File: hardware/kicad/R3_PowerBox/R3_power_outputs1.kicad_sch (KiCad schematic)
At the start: 7 parts, among them J10 BATTERY / CHARGER TELEMETRY, J2 DIGITAL POWER OUT, J3 ISOLATED POWER OUT, J4 CONTROL / SERVICE, J5 PRIMARY AUX DNP, J6 ISOLATED AUX DNP

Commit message: Finalize R3 PowerBox pre-placement corrections
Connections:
- net PD_CONTRACT_12V_N: now reaches J10.10
- net PD_ALERT_N: now reaches J10.9
- no-connect marks 7 -> 5

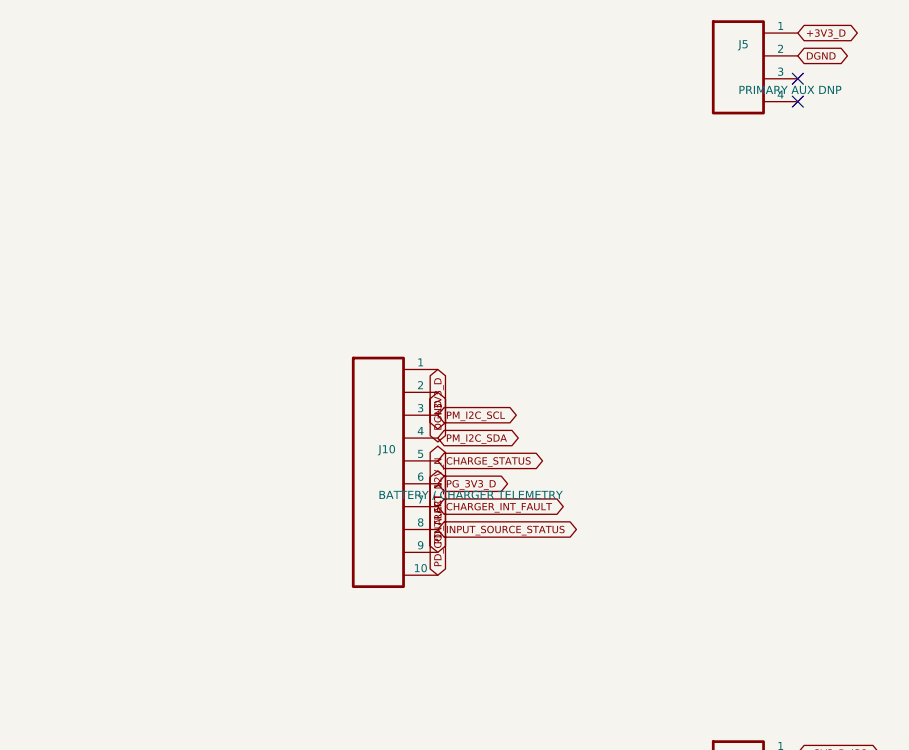
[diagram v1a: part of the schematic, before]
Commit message: Finalize R3 PowerBox pre-routing placement
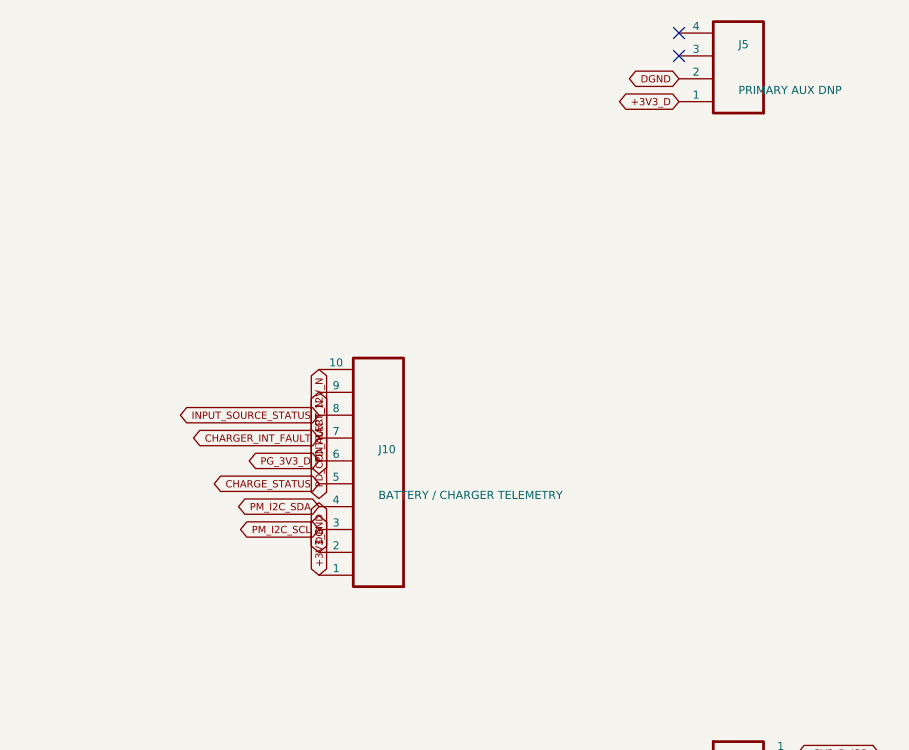
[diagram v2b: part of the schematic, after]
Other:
- moved on the sheet: J10, J5

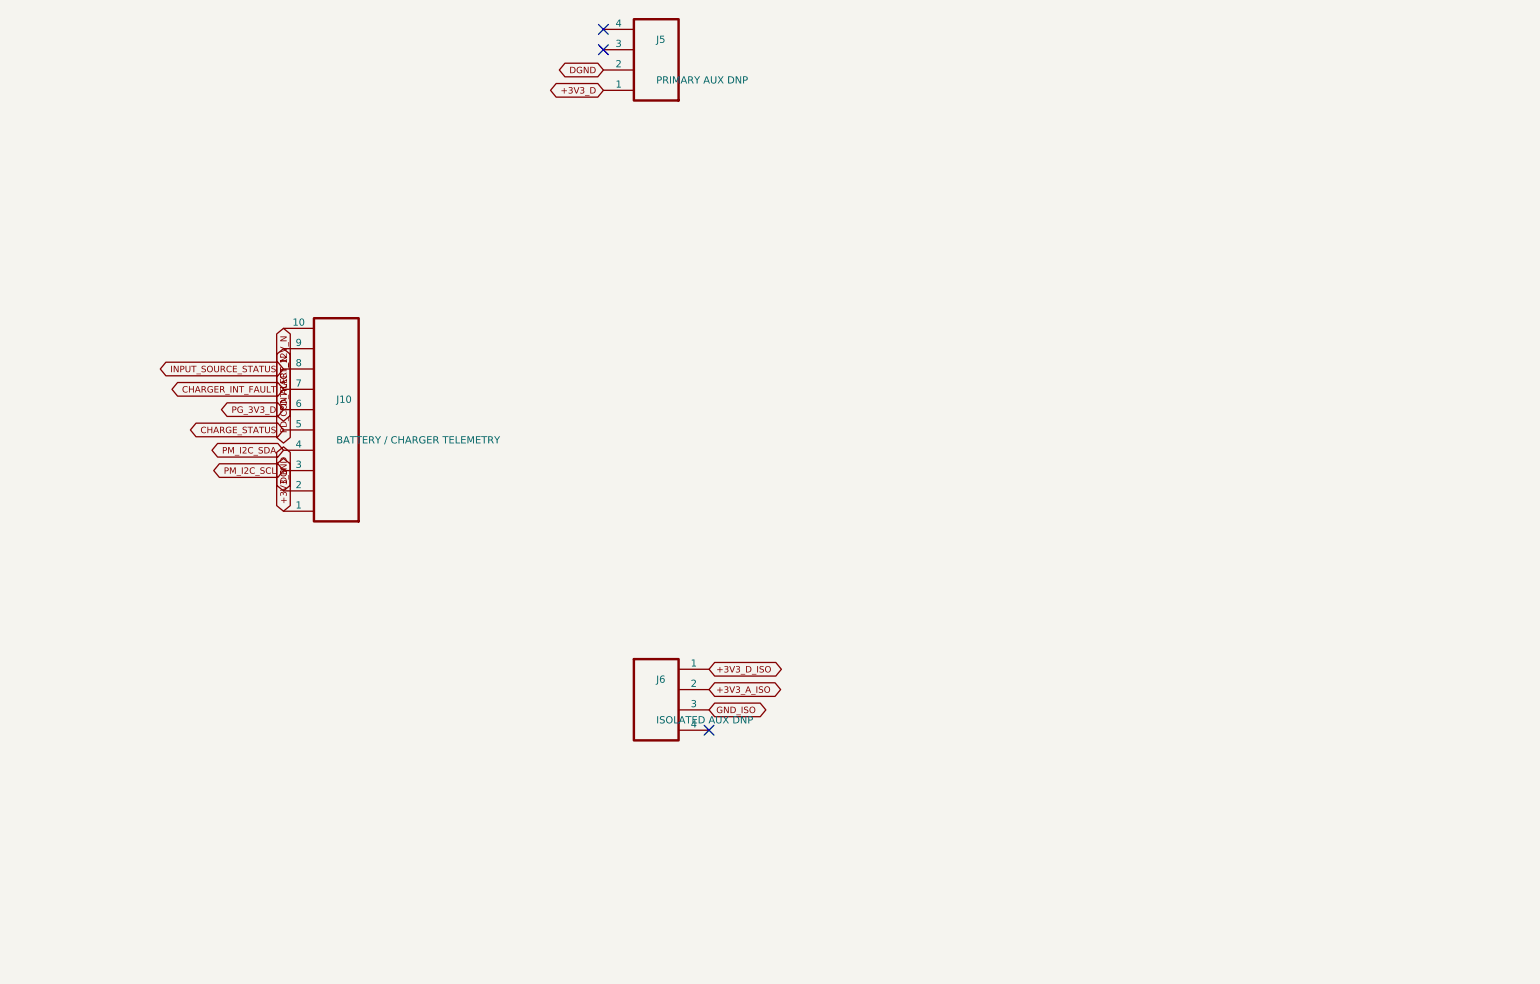
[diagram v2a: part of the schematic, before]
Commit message: Finalize R3 PowerBox user power controls
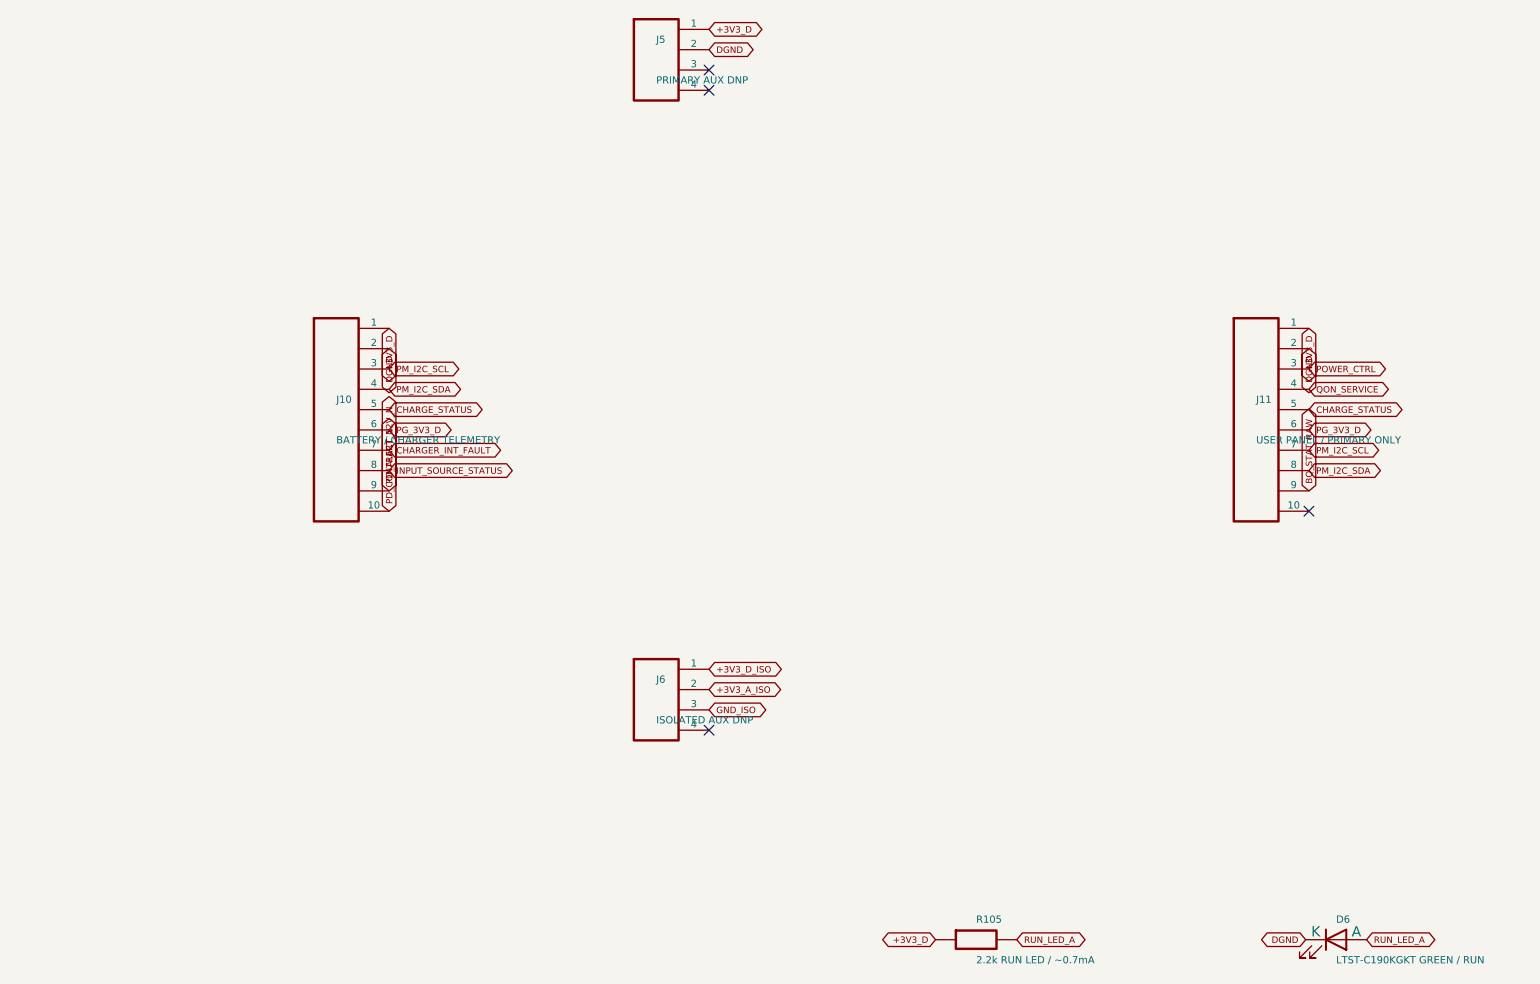
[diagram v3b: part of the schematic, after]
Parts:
- added D6: LTST-C190KGKT GREEN / RUN, LED_SMD:LED_0603_1608Metric, symbol Device:LED
- added J11: USER PANEL / PRIMARY ONLY, Connector_Molex:Molex_Micro-Fit_3.0_43650-1000_1x10_P3.00mm_Horizontal, symbol R3_POWER_GEN:CONN10
- added R105: 2.2k RUN LED / ~0.7mA, Resistor_SMD:R_0603_1608Metric, symbol R3_POWER_GEN:R
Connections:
- net +3V3_D: now also J11.1, R105.1
- net CHARGE_STATUS: now also J11.5
- net DGND: now also D6.1 (K), J11.2
- net PG_3V3_D: now also J11.6
- net PM_I2C_SCL: now also J11.7
- net PM_I2C_SDA: now also J11.8
- new net BQ_STAT_RAW: J11.9
- new net POWER_CTRL: J11.3
- new net QON_SERVICE: J11.4
- new net RUN_LED_A: D6.2 (A), R105.2
- no-connect marks 5 -> 6
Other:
- moved on the sheet: J10, J5

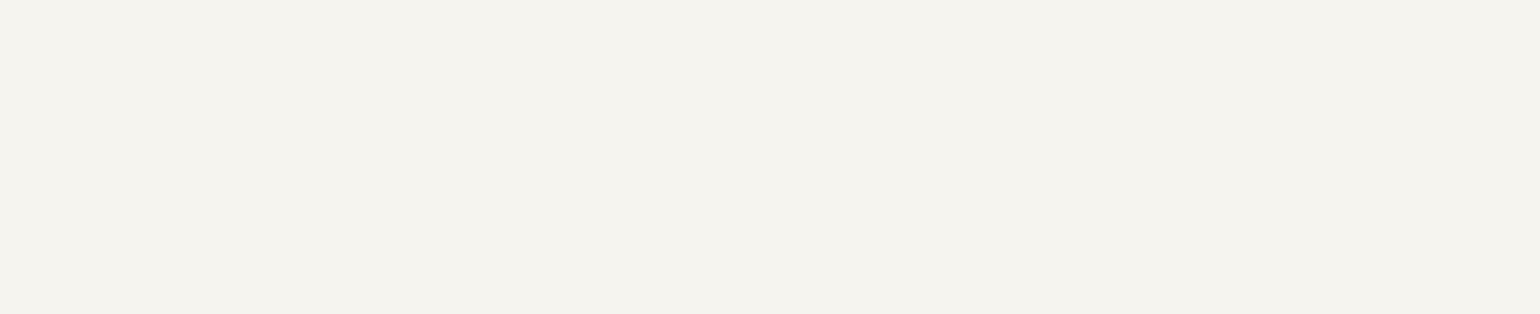
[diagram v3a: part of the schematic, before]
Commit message: Finalize R3 PowerBox mechanical interconnect
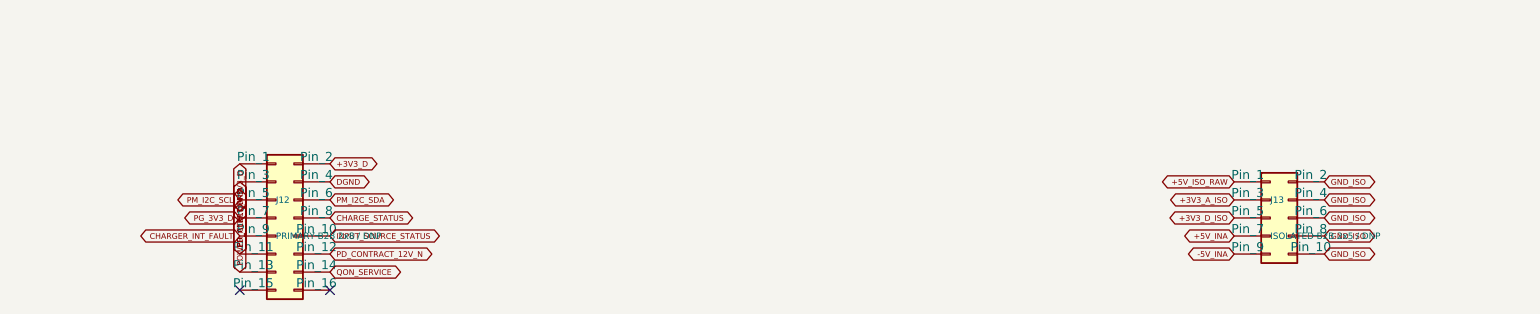
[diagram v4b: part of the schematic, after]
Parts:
- added J12: PRIMARY B2B 2x8 / DNP, Connector_PinHeader_2.54mm:PinHeader_2x08_P2.54mm_Vertical, symbol Connector_Generic:Conn_02x08_Odd_Even
- added J13: ISOLATED B2B 2x5 / DNP, Connector_PinHeader_2.54mm:PinHeader_2x05_P2.54mm_Vertical, symbol Connector_Generic:Conn_02x05_Odd_Even
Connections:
- net +3V3_A_ISO: now also J13.3 (Pin_3)
- net +3V3_D: now also J12.1 (Pin_1), J12.2 (Pin_2)
- net +3V3_D_ISO: now also J13.5 (Pin_5)
- net +5V_INA: now also J13.7 (Pin_7)
- net +5V_ISO_RAW: now also J13.1 (Pin_1)
- net -5V_INA: now also J13.9 (Pin_9)
- net CHARGER_INT_FAULT: now also J12.9 (Pin_9)
- net CHARGE_STATUS: now also J12.8 (Pin_8)
- net DGND: now also J12.3 (Pin_3), J12.4 (Pin_4)
- net GND_ISO: now also J13.10 (Pin_10), J13.2 (Pin_2), J13.4 (Pin_4), J13.6 (Pin_6), J13.8 (Pin_8)
- net INPUT_SOURCE_STATUS: now also J12.10 (Pin_10)
- net PD_ALERT_N: now also J12.11 (Pin_11)
- net PD_CONTRACT_12V_N: now also J12.12 (Pin_12)
- net PG_3V3_D: now also J12.7 (Pin_7)
- net PM_I2C_SCL: now also J12.5 (Pin_5)
- net PM_I2C_SDA: now also J12.6 (Pin_6)
- net POWER_CTRL: now also J12.13 (Pin_13)
- net QON_SERVICE: now also J12.14 (Pin_14)
- no-connect marks 6 -> 8
